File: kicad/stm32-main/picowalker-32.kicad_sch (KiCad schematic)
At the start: 18 parts, among them IC1 TFBS4711-TT1, IC2 M95512-DRMN8TP_K, IC3 IS25WP128F-JBLE, J1 DBG_HDR, J2 PROGRAM_HDR, SW1 BUT_L, SW2 BUT_M, SW3 BUT_R, U3 BMA400

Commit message: hw: screen updates
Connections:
- no-connect marks 8 -> 9
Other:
- sheet screen ports: added PWR_EN, TP_RST; removed none
- note added: "If unused, leave open"
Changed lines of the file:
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@@
   (no_connect (at 171.45 80.01))
   (no_connect (at 30.48 105.41))
+  (no_connect (at 171.45 77.47))
   (no_connect (at 171.45 82.55))
   (no_connect (at 255.27 58.42))
@@
     (stroke (width 0) (type default))
   )
+  (wire (pts (xy 135.89 82.55) (xy 138.43 82.55))
+    (stroke (width 0) (type default))
+  )
   (wire (pts (xy 96.52 43.18) (xy 111.76 43.18))
     (stroke (width 0) (type default))
@@
     (stroke (width 0) (type default))
   )
+  (wire (pts (xy 166.37 77.47) (xy 171.45 77.47))
+    (stroke (width 0) (type default))
+  )
   (wire (pts (xy 166.37 82.55) (xy 171.45 82.55))
     (stroke (width 0) (type default))
@@
     (stroke (width 0) (type default))
   )
-  (wire (pts (xy 166.37 72.39) (xy 172.72 72.39))
+  (wire (pts (xy 166.37 72.39) (xy 177.8 72.39))
     (stroke (width 0) (type default))
   )
@@
   )
   (text_box "Screen"
-    (at 118.11 55.88 0) (size 62.23 36.83)
+    (at 109.22 55.88 0) (size 91.44 36.83)
     (stroke (width 0) (type default))
     (fill (type none))
@@
     (fill (type none))
     (effects (font (size 1.27 1.27)) (justify left top))
+  )
+  (text "If unused, leave open" (at 176.53 82.55 0)
+    (effects (font (size 1.27 1.27)) (justify left bottom))
   )
   (text "1.2V - 3.6V" (at 227.33 19.05 0)
@@
     (effects (font (size 1.27 1.27)) (justify right))
     (property "Intersheetrefs" "${INTERSHEET_REFS}" (at 20.9823 179.07 0)
+      (effects (font (size 1.27 1.27)) (justify right) hide)
+    )
+  )
+  (global_label "SCREEN_PWR_EN" (shape input) (at 135.89 82.55 180) (fields_autoplaced)
+    (effects (font (size 1.27 1.27)) (justify right))
+    (property "Intersheetrefs" "${INTERSHEET_REFS}" (at 117.1207 82.55 0)
       (effects (font (size 1.27 1.27)) (justify right) hide)
     )
@@
     )
   )
-  (symbol (lib_id "power:GND") (at 172.72 72.39 0) (unit 1)
-    (in_bom yes) (on_board yes) (dnp no) (fields_autoplaced)
-    (property "Reference" "#PWR047" (at 172.72 78.74 0)
-      (effects (font (size 1.27 1.27)) hide)
-    )
-    (property "Value" "GND" (at 172.72 77.47 0)
-      (effects (font (size 1.27 1.27)))
-    )
-    (property "Footprint" "" (at 172.72 72.39 0)
-      (effects (font (size 1.27 1.27)) hide)
-    )
-    (property "Datasheet" "" (at 172.72 72.39 0)
+  (symbol (lib_id "power:GND") (at 177.8 72.39 0) (unit 1)
+    (in_bom yes) (on_board yes) (dnp no) (fields_autoplaced)
+    (property "Reference" "#PWR047" (at 177.8 78.74 0)
+      (effects (font (size 1.27 1.27)) hide)
+    )
+    (property "Value" "GND" (at 177.8 77.47 0)
+      (effects (font (size 1.27 1.27)))
+    )
+    (property "Footprint" "" (at 177.8 72.39 0)
+      (effects (font (size 1.27 1.27)) hide)
+    )
+    (property "Datasheet" "" (at 177.8 72.39 0)
       (effects (font (size 1.27 1.27)) hide)
     )
@@
       (effects (font (size 1.27 1.27)) (justify right))
     )
-    (instances
+    (pin "TP_RST" input (at 166.37 77.47 0)
+      (effects (font (size 1.27 1.27)) (justify right))
+    )
+    (pin "PWR_EN" input (at 138.43 82.55 180)
+      (effects (font (size 1.27 1.27)) (justify left))
+    )
+    (instances

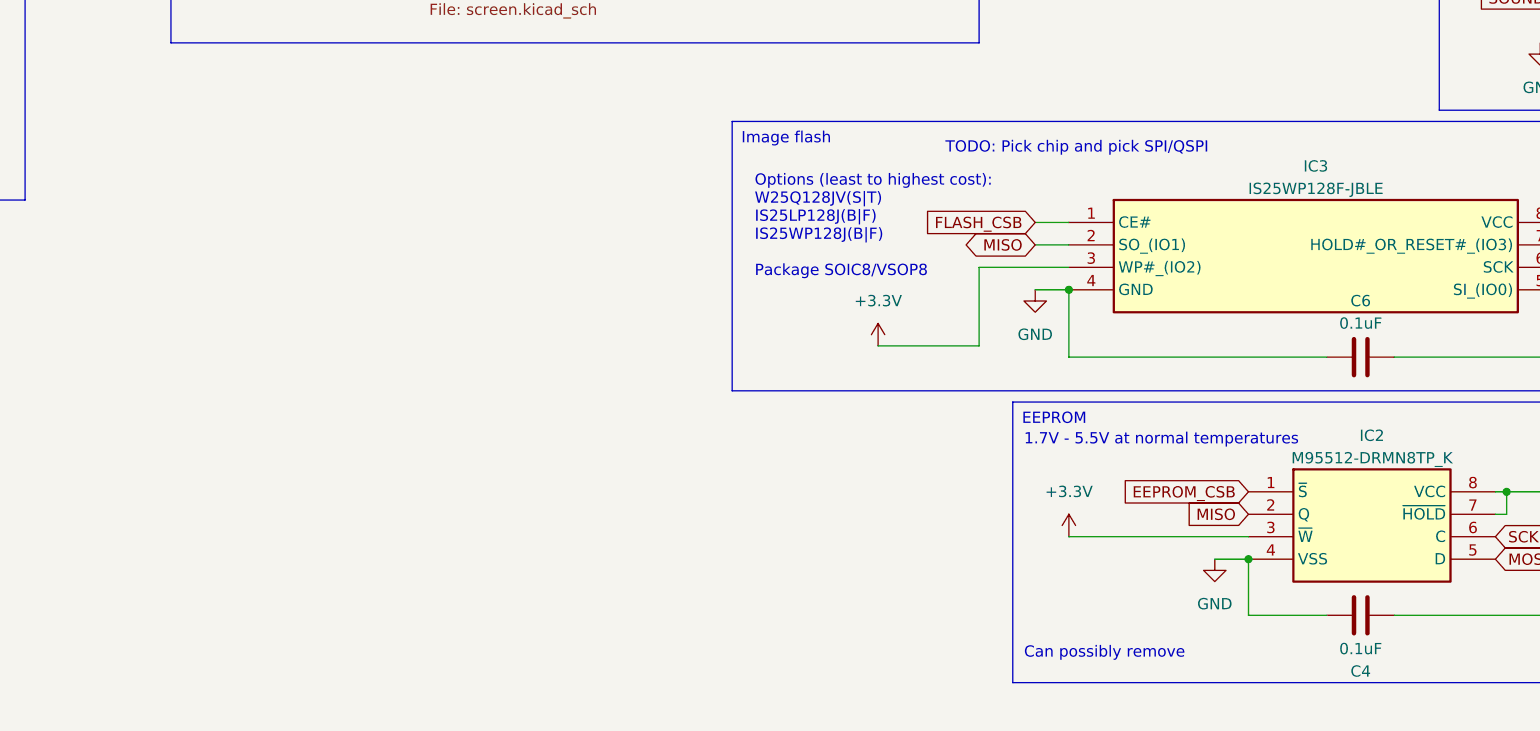
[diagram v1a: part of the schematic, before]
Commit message: hw: update screen stuff
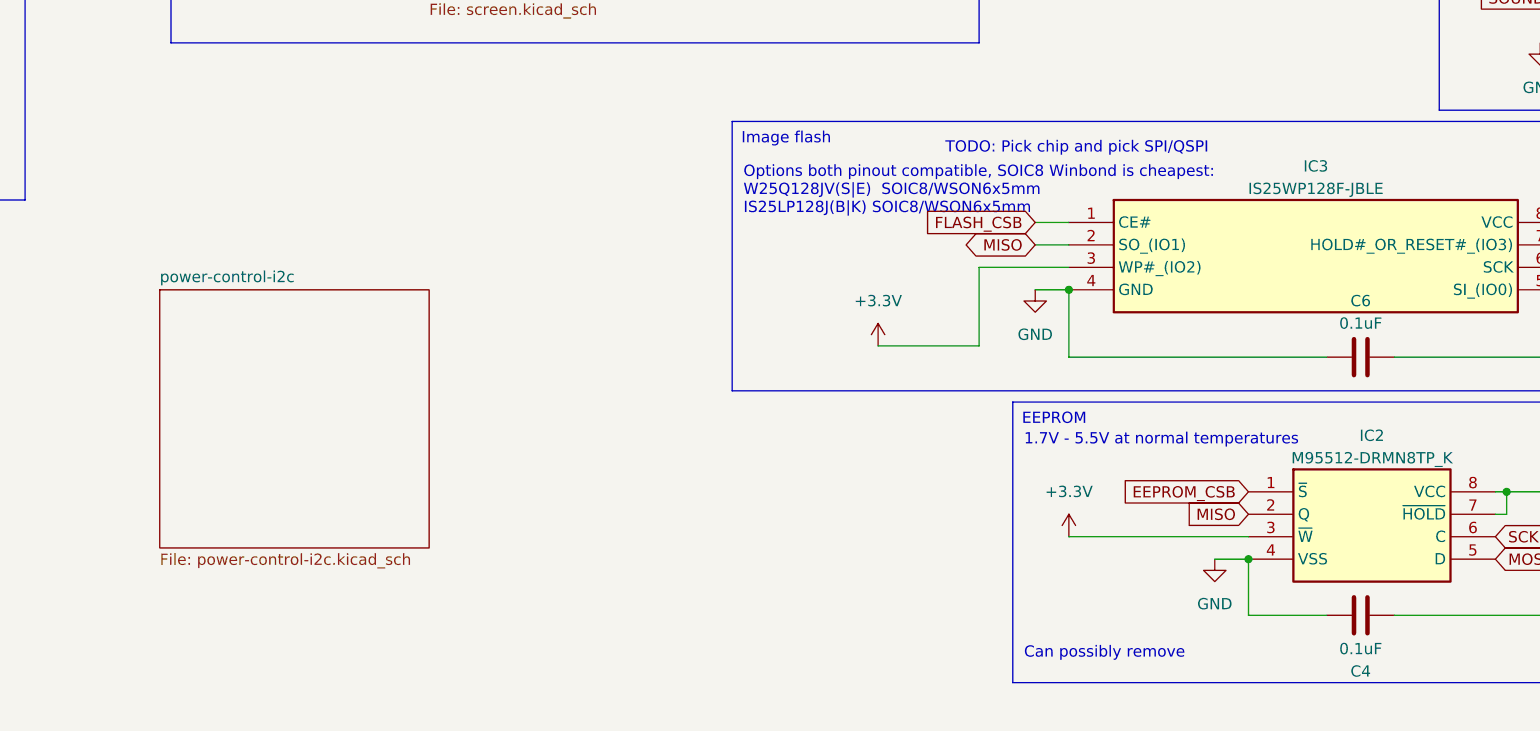
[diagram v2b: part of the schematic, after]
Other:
- added sheet power-control-i2c (power-control-i2c.kicad_sch)
- note added: "Options both pinout compatible, SOIC8 Winbond is cheapest: W25Q128JV(S|E) SOIC8/WSON6x5mm IS25LP128J(B|K) SOIC8/WSON6x5mm"
- note removed: "Options (least to highest cost): W25Q128JV(S|T) IS25LP128J(B|F) IS25WP128J(B|F) Package SOIC8/VSOP8"
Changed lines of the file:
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@@
     (effects (font (size 1.27 1.27)) (justify left bottom))
   )
-  (text "Options (least to highest cost):\nW25Q128JV(S|T)\nIS25LP128J(B|F)\nIS25WP128J(B|F)\n\nPackage SOIC8/VSOP8"
-    (at 175.26 119.38 0)
+  (text "Options both pinout compatible, SOIC8 Winbond is cheapest:\nW25Q128JV(S|E)  SOIC8/WSON6x5mm\nIS25LP128J(B|K) SOIC8/WSON6x5mm\n\n"
+    (at 173.99 114.3 0)
     (effects (font (size 1.27 1.27)) (justify left bottom))
   )
@@
       )
     )
+  )
+  (sheet (at 107.95 120.65) (size 30.48 29.21) (fields_autoplaced)
+    (stroke (width 0.1524) (type solid))
+    (fill (color 0 0 0 0.0000))
+    (property "Sheetname" "power-control-i2c" (at 107.95 119.9384 0)
+      (effects (font (size 1.27 1.27)) (justify left bottom))
+    )
+    (property "Sheetfile" "power-control-i2c.kicad_sch" (at 107.95 150.4446 0)
+      (effects (font (size 1.27 1.27)) (justify left top))
+    )
+    (instances
+      (project "picowalker-32"
+        (path "/17fa99ff-0271-4e85-b8d9-a0357d961230" (page "5"))
+      )
+    )
